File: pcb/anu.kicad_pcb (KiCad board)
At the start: 2 copper layers, 55.2 x 55.5 mm, 13 parts, among them J1 battery connector, SW1 SW_PUSH, SW2 SW_PUSH, SW3 SW_PUSH, SW4 SW_SPDT, U1 ProMicro_r, X1 FJ08K-S

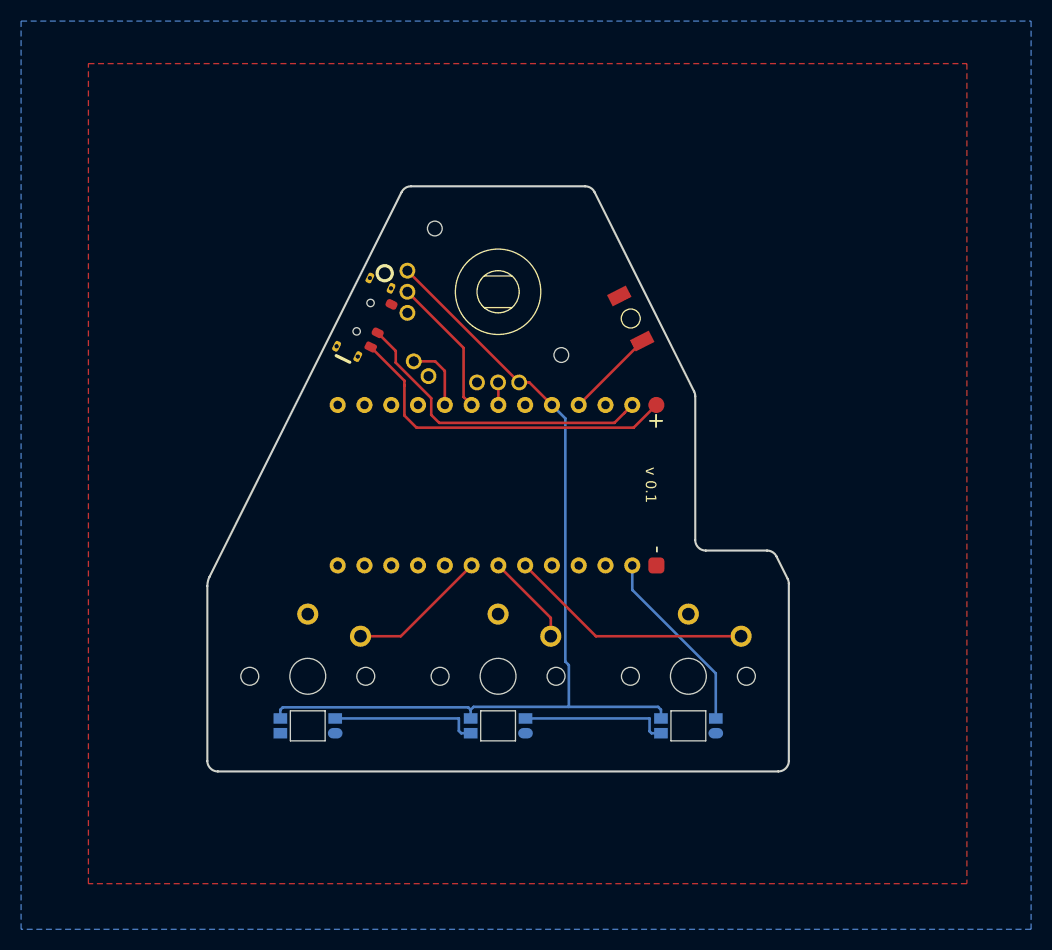
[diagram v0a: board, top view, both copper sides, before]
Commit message: add screws & panels
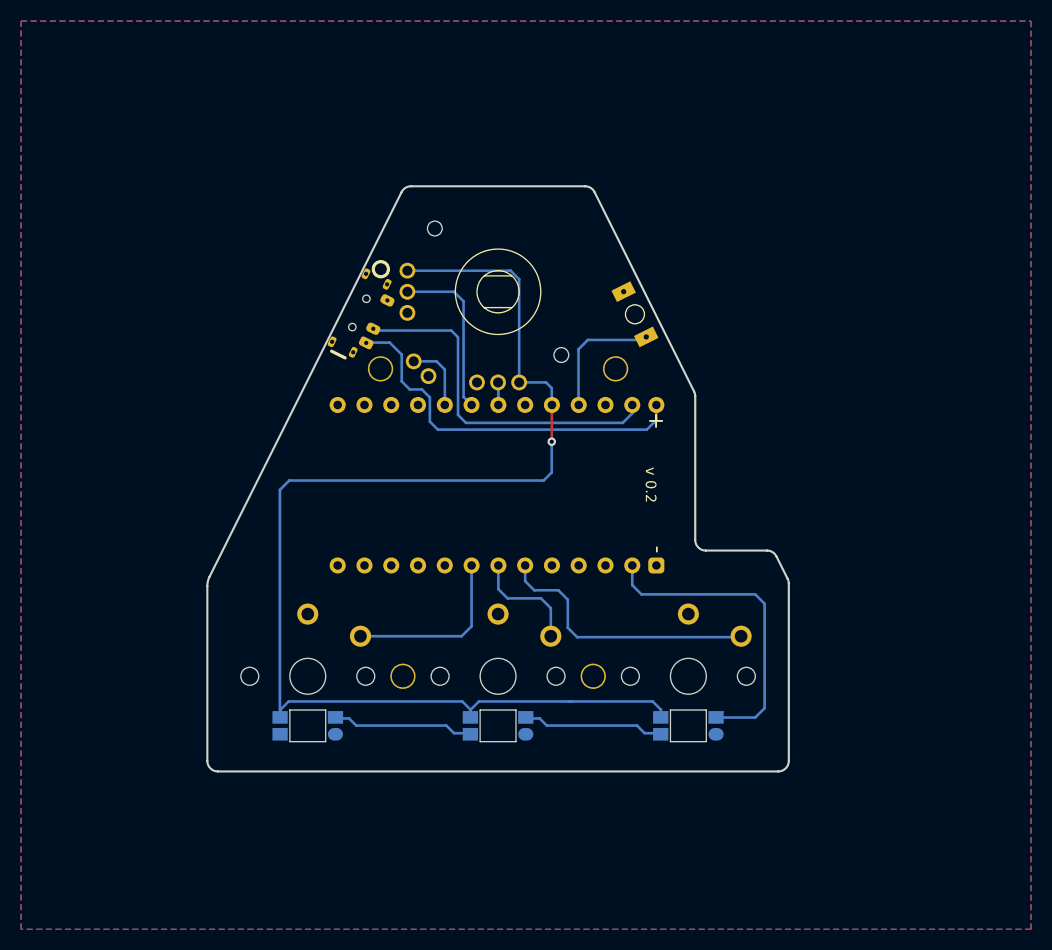
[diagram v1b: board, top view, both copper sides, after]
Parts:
- added H1: Hole, enki_lib:HOLE, F.Cu at (142.0, 137.8)
- added H1: Hole, enki_lib:HOLE, F.Cu at (139.8, 108.7)
- added H1: Hole, enki_lib:HOLE, F.Cu at (160.0, 137.8)
- added H1: Hole, enki_lib:HOLE, F.Cu at (162.1, 108.7)
- moved G2 0.60 mm to (151.6, 119.7)
- moved SW4 0.57 mm to (137.8, 103.4), turned to 63.5 degrees
- moved RSW1 0.57 mm to (164.0, 103.5), turned to 116.5 degrees
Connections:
- LED1 pad 2: (no net) -> unconnected-(LED1-DOUT-Pad2)
- SW4 pad 1: (no net) -> unconnected-(SW4-A-Pad1)
- U1 pad 10: (no net) -> unconnected-(U1-E6/7-Pad10)
- U1 pad 11: (no net) -> unconnected-(U1-B4/8-Pad11)
- U1 pad 12: (no net) -> unconnected-(U1-B5/9-Pad12)
- U1 pad 13: (no net) -> unconnected-(U1-10/B6-Pad13)
- U1 pad 14: (no net) -> unconnected-(U1-16/B2-Pad14)
- U1 pad 15: (no net) -> unconnected-(U1-14/B3-Pad15)
- U1 pad 16: (no net) -> unconnected-(U1-15/B1-Pad16)
- U1 pad 2: (no net) -> unconnected-(U1-D2/RX1-Pad2)
- U1 pad 20: (no net) -> unconnected-(U1-A3/F4-Pad20)
- U1 pad 8: (no net) -> unconnected-(U1-C6/5-Pad8)
- U1 pad 9: (no net) -> unconnected-(U1-D7/6-Pad9)
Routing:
- net VCC: track 87.3 -> 120.3 mm, vias 0 -> 1
- net LED: track 17.8 -> 30.0 mm
- net VBAT: track 30.0 -> 33.7 mm
- net sw1: track 13.3 -> 16.7 mm
- net reset: track 8.56 -> 11.7 mm
- net Net-(J1-Pin_1): track 33.1 -> 35.7 mm
- net analogX: track 13.3 -> 15.8 mm
- net sw3: track 23.3 -> 25.8 mm
- net sw2: track 8.77 -> 10.6 mm
- net Net-(LED2-DIN): track 14.1 -> 13.4 mm
- net Net-(LED1-DIN): track 14.1 -> 13.4 mm
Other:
- board text added: "v 0.2"
- board text removed: "v 0.1"
